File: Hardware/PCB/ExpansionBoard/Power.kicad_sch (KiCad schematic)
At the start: 4 parts, among them IC401 TPS7B8633QDDARQ1, J401 Conn_01x02_Pin

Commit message: added USB and Powerseitcher
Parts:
- added C403: 10u, symbol Device:C_Small
- added C404: 0.1u, symbol Device:C_Small
- added C405: NC, symbol Device:C_Small
- added D401: D, symbol Device:D
- added IC402: MP62550DJ-LF-Z, SOT95P280X100-6N, symbol SamacSys_Parts:MP62550DJ-LF-Z
- added R401, R402, R403: 10k, symbol Device:R_Small
- added R404: 52.3k 1%ACC, symbol Device:R_Small
- added R405: 0, symbol Device:R_Small
- added TP401: TestPoint, symbol Connector:TestPoint
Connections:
- net GND: now also C405.1, R403.2, R404.2
- net at C402.1, IC401.7 (EN), IC401.8 (IN): now also D401.1 (K), R405.1; no longer J401.1 (Pin_1)
- new net: C405.2, IC402.6 (OUT), R405.2
- new net: D401.2 (A), J401.1 (Pin_1), R402.1
- new net: IC402.3 (EN), R402.2, R403.1
- new net: IC402.4 (~{FLAG}), R401.1, TP401.1
- new net: C403.2, C404.2, IC402.2 (GND)
- new net: IC402.5 (ILIM), R404.1
- new net +5V: C403.1, C404.1, IC402.1 (IN), R401.2
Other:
- moved on the sheet: J401

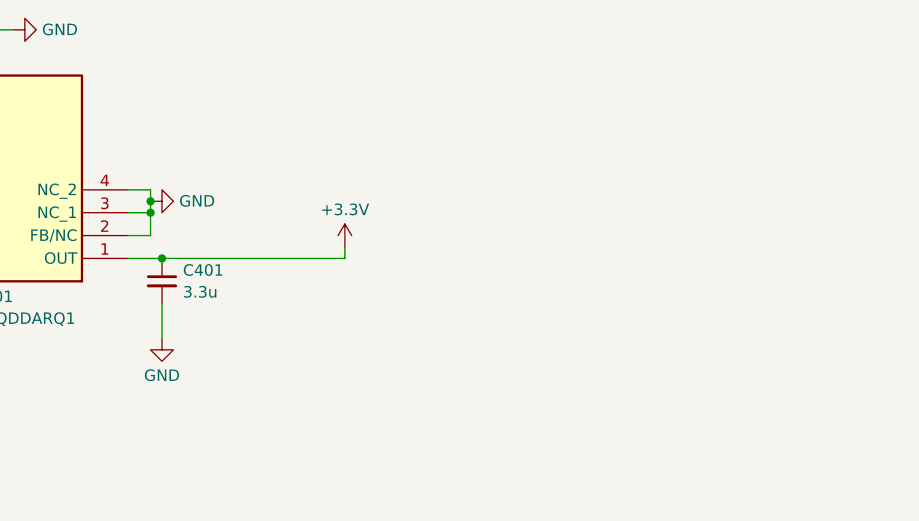
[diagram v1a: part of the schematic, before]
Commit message: DONE: PWR LED MISSING AND AIRSPEED
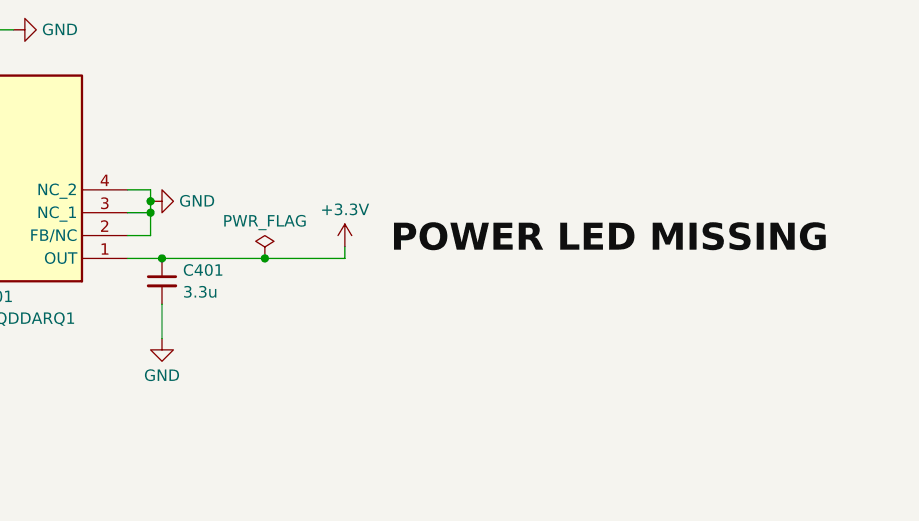
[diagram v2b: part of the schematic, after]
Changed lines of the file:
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@@
+	)
+	(junction
+		(at 172.72 91.44)
+		(diameter 0)
+		(color 0 0 0 0)
 	)
 	(junction
@@
 	(wire
 		(pts
-			(xy 161.29 91.44) (xy 181.61 91.44)
+			(xy 161.29 91.44) (xy 172.72 91.44)
 		)
 		(stroke
@@
 	(wire
 		(pts
+			(xy 172.72 91.44) (xy 181.61 91.44)
+		)
+		(stroke
+			(width 0)
+			(type default)
+		)
+	)
+	(wire
+		(pts
 			(xy 121.92 97.79) (xy 121.92 100.33)
 		)
@@
 			(width 0)
 			(type default)
+		)
+	)
+	(label "POWER LED MISSING"
+		(at 186.69 91.44 0)
+		(fields_autoplaced yes)
+		(effects
+			(font
+				(size 3 3)
+				(thickness 0.254)
+				(bold yes)
+				(color 255 0 0 1)
+			)
+			(justify left bottom)
 		)
 	)
@@
 					(unit 1)
 				)
+			)
+		)
+	)
+	(symbol
+		(lib_id "power:PWR_FLAG")
+		(at 172.72 91.44 0)
+		(unit 1)
+		(exclude_from_sim no)
+		(in_bom yes)
+		(on_board yes)
+		(dnp no)
+		(fields_autoplaced yes)
+		(property "Reference" "#FLG0402"
+			(at 172.72 89.535 0)
+			(effects
+				(font
+					(size 1.27 1.27)
+				)
+				(hide yes)
+			)
+		)
+		(property "Value" "PWR_FLAG"
+			(at 172.72 87.3069 0)
+			(effects
+				(font
+					(size 1.27 1.27)
+				)
+			)
+		)
+		(property "Footprint" ""
+			(at 172.72 91.44 0)
+			(effects
+				(font
+					(size 1.27 1.27)
+				)
+				(hide yes)
+			)
+		)
+		(property "Datasheet" "~"
+			(at 172.72 91.44 0)
+			(effects
+				(font
+					(size 1.27 1.27)
+				)
+				(hide yes)
+			)
+		)
+		(property "Description" "Special symbol for telling ERC where power comes from"
+			(at 172.72 91.44 0)
+			(effects
+				(font
+					(size 1.27 1.27)
+				)
+				(hide yes)
+			)
+		)
+		(pin "1"
+		)
+		(instances
+			(project "ExpansionBoard"
+				(path "/fb49e4b5-d7b7-45bf-8a57-314a3950416b/543fedc8-8e40-46c9-a18c-68a6ffedc4b3"
+					(reference "#FLG0402")
+					(unit 1)
+				)

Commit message: finished schema
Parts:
- removed D401: D, symbol Device:D
- added D401: LED, SamacSys_Parts:LEDC2012X80N, symbol Device:LED
- added D402: LSM115JE3_TR13, DIOM5436X330N, symbol SamacSys_Parts:LSM115JE3_TR13
- added R406: 68, Resistor_SMD:R_0805_2012Metric_Pad1.20x1.40mm_HandSolder, symbol Device:R_Small
- C401, C402, C403, C404, C405: footprint (none) -> Capacitor_SMD:C_0805_2012Metric_Pad1.18x1.45mm_HandSolder
- R401, R402, R403, R404, R405: footprint (none) -> Resistor_SMD:R_0805_2012Metric_Pad1.20x1.40mm_HandSolder
- TP401: footprint (none) -> TestPoint:TestPoint_Pad_D3.0mm
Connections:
- net +3.3V: now also R406.1
- net GND: now also D401.1 (K)
- net at C402.1, IC401.7 (EN), IC401.8 (IN)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: now also D402.1 (K)
- net at J401.1 (Pin_1), R402.1: now also D402.2 (A)
- new net: D401.2 (A), R406.2

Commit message: to pcb
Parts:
- D402: footprint DIOM5436X330N -> SamacSys_Parts:DIOM5436X330N
- IC401: footprint SOIC127P600X170-9N -> SamacSys_Parts:SOIC127P600X170-9N
- IC402: footprint SOT95P280X100-6N -> SamacSys_Parts:SOT95P280X100-6N
- TP401: footprint TestPoint:TestPoint_Pad_D3.0mm -> TestPoint:TestPoint_Pad_D1.5mm
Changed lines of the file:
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@@
 			)
 		)
-		(property "Footprint" "SOIC127P600X170-9N"
+		(property "Footprint" "SamacSys_Parts:SOIC127P600X170-9N"
 			(at 130.81 -3.48 0)
 			(effects
@@
 			)
 		)
-		(property "Footprint" "TestPoint:TestPoint_Pad_D3.0mm"
+		(property "Footprint" "TestPoint:TestPoint_Pad_D1.5mm"
 			(at 107.95 128.27 0)
 			(effects
@@
 			)
 		)
-		(property "Footprint" "SOT95P280X100-6N"
+		(property "Footprint" "SamacSys_Parts:SOT95P280X100-6N"
 			(at 104.14 213.03 0)
 			(effects
@@
 			)
 		)
-		(property "Footprint" "DIOM5436X330N"
+		(property "Footprint" "SamacSys_Parts:DIOM5436X330N"
 			(at 72.39 -2.21 0)
 			(effects

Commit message: finished pcb layout
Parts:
- added H401, H403, H404: MountingHole, MountingHole:MountingHole_2.2mm_M2, symbol Mechanical:MountingHole
- D402: footprint SamacSys_Parts:DIOM5436X330N -> DIOM5436X330N
- IC401: footprint SamacSys_Parts:SOIC127P600X170-9N -> SOIC127P600X170-9N
- IC402: footprint SamacSys_Parts:SOT95P280X100-6N -> SOT95P280X100-6N
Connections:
- net GND: now also C403.2, C404.2, IC402.2 (GND)
- net VDD: now reaches D402.2 (A), J401.1 (Pin_1), R402.1

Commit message: finsihed pcb
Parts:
- D402: footprint DIOM5436X330N -> SamacSys_Parts:DIOM5436X330N
- IC401: footprint SOIC127P600X170-9N -> SamacSys_Parts:SOIC127P600X170-9N
- IC402: footprint SOT95P280X100-6N -> SamacSys_Parts:SOT95P280X100-6N
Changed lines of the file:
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@@
 			)
 		)
-		(property "Footprint" "SOIC127P600X170-9N"
+		(property "Footprint" "SamacSys_Parts:SOIC127P600X170-9N"
 			(at 130.81 -3.48 0)
 			(effects
@@
 			)
 		)
-		(property "Footprint" "SOT95P280X100-6N"
+		(property "Footprint" "SamacSys_Parts:SOT95P280X100-6N"
 			(at 104.14 213.03 0)
 			(effects
@@
 			)
 		)
-		(property "Footprint" "DIOM5436X330N"
+		(property "Footprint" "SamacSys_Parts:DIOM5436X330N"
 			(at 72.39 -2.21 0)
 			(effects
